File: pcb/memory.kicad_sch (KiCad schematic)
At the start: 3 parts, among them U10 MT41K256M16TW-107:P TR, U9 MX25L12835F

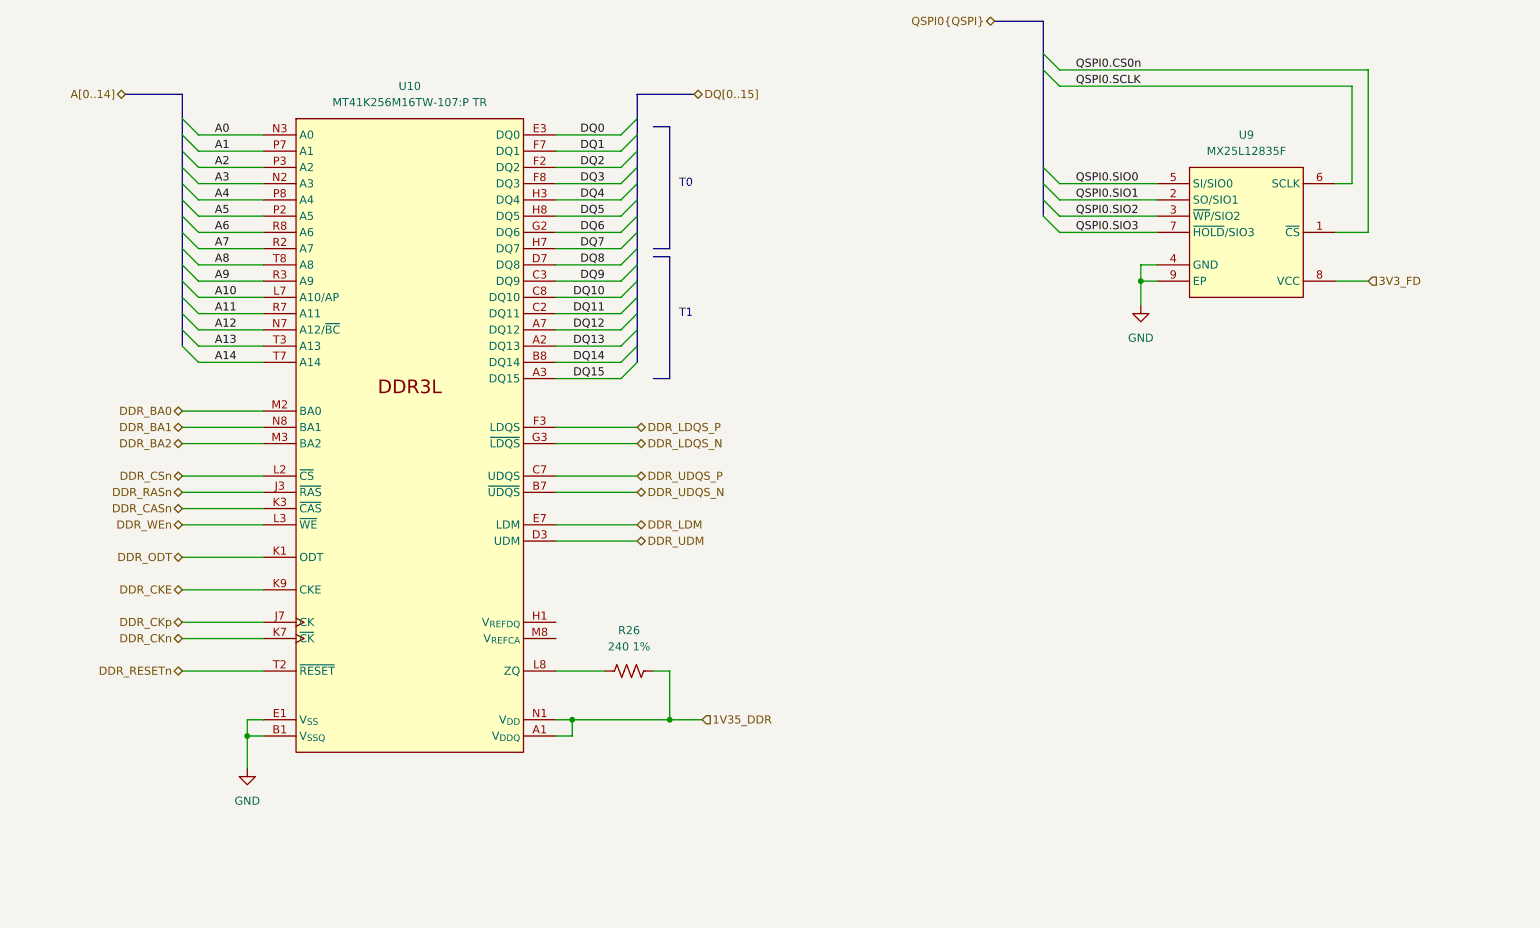
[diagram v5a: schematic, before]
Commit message: real ddr pinout done
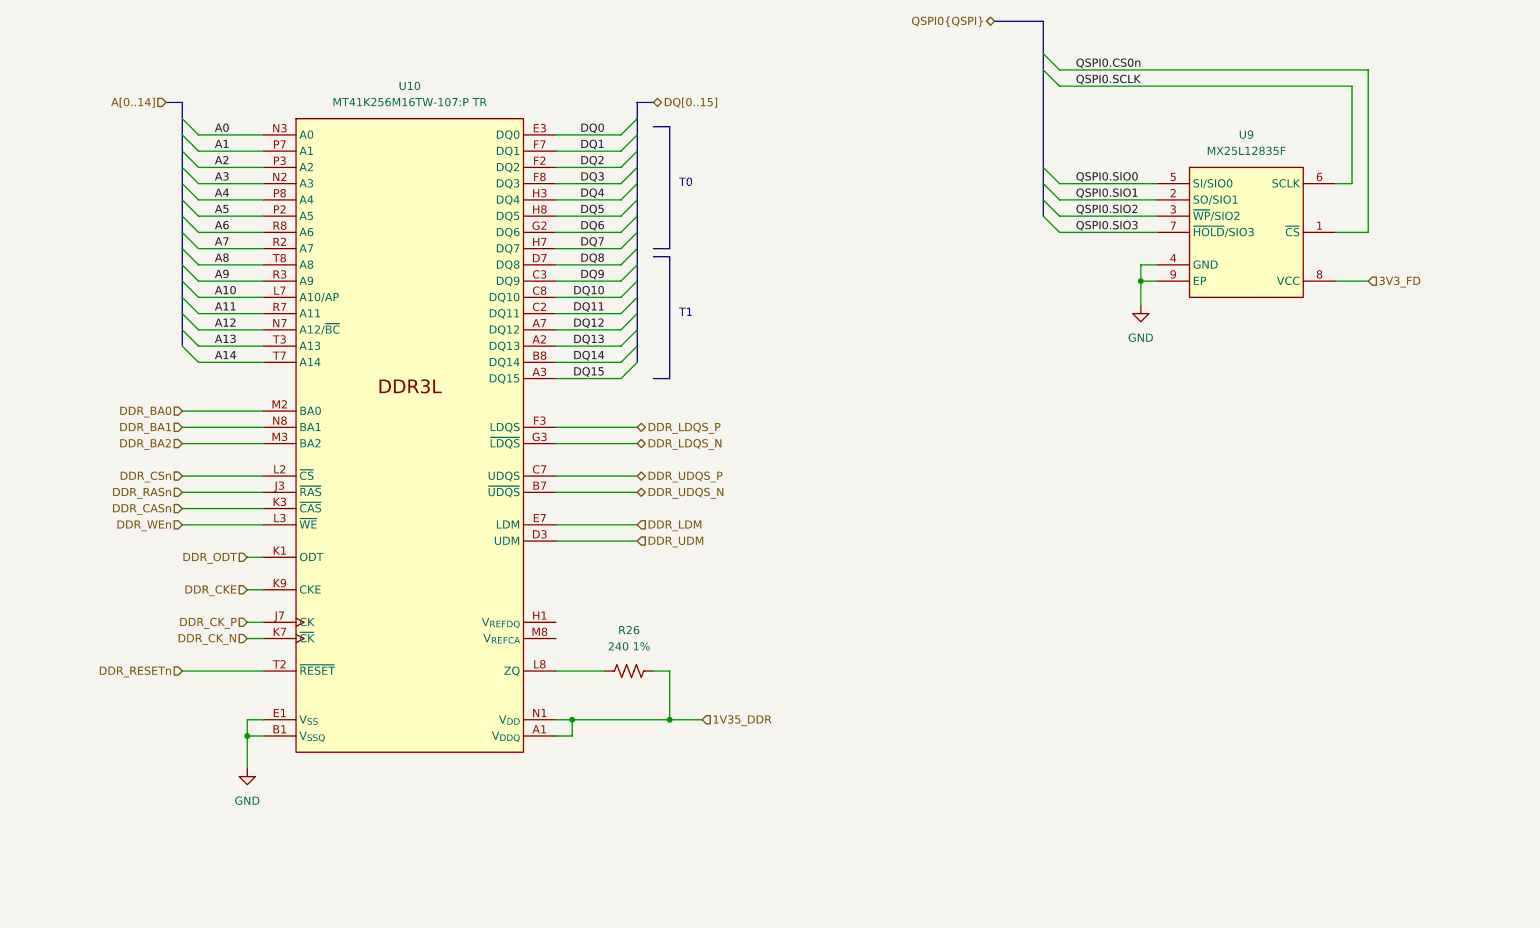
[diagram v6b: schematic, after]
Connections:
- net DDR_CKn renamed DDR_CK_N
- net DDR_CKp renamed DDR_CK_P
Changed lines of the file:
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@@
 	(wire
 		(pts
-			(xy 71.12 114.3) (xy 83.82 114.3)
+			(xy 81.28 114.3) (xy 83.82 114.3)
 		)
 		(stroke
@@
 		)
 	)
-	(bus
+	(wire
 		(pts
-			(xy 71.12 36.83) (xy 62.23 36.83)
+			(xy 73.66 76.2) (xy 83.82 76.2)
 		)
 		(stroke
@@
 		)
 	)
-	(wire
+	(bus
 		(pts
-			(xy 73.66 76.2) (xy 83.82 76.2)
+			(xy 142.24 38.1) (xy 142.24 40.64)
 		)
 		(stroke
@@
 	(wire
 		(pts
-			(xy 71.12 121.92) (xy 83.82 121.92)
+			(xy 81.28 121.92) (xy 83.82 121.92)
 		)
 		(stroke
@@
 	(wire
 		(pts
-			(xy 71.12 109.22) (xy 83.82 109.22)
+			(xy 81.28 109.22) (xy 83.82 109.22)
 		)
 		(stroke
@@
 		)
 	)
-	(bus
-		(pts
-			(xy 142.24 40.64) (xy 142.24 36.83)
-		)
-		(stroke
-			(width 0)
-			(type default)
-		)
-	)
 	(wire
 		(pts
@@
 	(bus
 		(pts
-			(xy 142.24 36.83) (xy 151.13 36.83)
-		)
-		(stroke
-			(width 0)
-			(type default)
-		)
-	)
-	(bus
-		(pts
 			(xy 142.24 63.5) (xy 142.24 60.96)
 		)
@@
 	(bus
 		(pts
-			(xy 71.12 40.64) (xy 71.12 36.83)
+			(xy 71.12 40.64) (xy 71.12 38.1)
 		)
 		(stroke
@@
 	(bus
 		(pts
+			(xy 68.58 38.1) (xy 71.12 38.1)
+		)
+		(stroke
+			(width 0)
+			(type default)
+		)
+	)
+	(bus
+		(pts
 			(xy 71.12 48.26) (xy 71.12 45.72)
 		)
@@
 		)
 	)
+	(bus
+		(pts
+			(xy 142.24 38.1) (xy 144.78 38.1)
+		)
+		(stroke
+			(width 0)
+			(type default)
+		)
+	)
 	(wire
 		(pts
@@
 	(wire
 		(pts
-			(xy 71.12 119.38) (xy 83.82 119.38)
+			(xy 81.28 119.38) (xy 83.82 119.38)
 		)
 		(stroke
@@
 		)
 	)
-	(hierarchical_label "DDR_UDM"
-		(shape bidirectional)
-		(at 142.24 106.68 0)
+	(hierarchical_label "DDR_BA0"
+		(shape input)
+		(at 71.12 86.36 180)
 		(effects
 			(font
 				(size 1.27 1.27)
 			)
-			(justify left)
+			(justify right)
 		)
 	)
-	(hierarchical_label "DDR_BA2"
+	(hierarchical_label "DQ[0..15]"
 		(shape bidirectional)
-		(at 71.12 91.44 180)
+		(at 144.78 38.1 0)
 		(effects
 			(font
 				(size 1.27 1.27)
+				(thickness 0.1588)
 			)
-			(justify right)
+			(justify left)
 		)
 	)
-	(hierarchical_label "A[0..14]"
-		(shape bidirectional)
-		(at 62.23 36.83 180)
+	(hierarchical_label "DDR_LDM"
+		(shape input)
+		(at 142.24 104.14 0)
 		(effects
 			(font
 				(size 1.27 1.27)
-				(thickness 0.1588)
 			)
-			(justify right)
+			(justify left)
 		)
 	)
-	(hierarchical_label "DDR_LDQS_P"
+	(hierarchical_label "DDR_UDQS_N"
 		(shape bidirectional)
-		(at 142.24 88.9 0)
+		(at 142.24 99.06 0)
 		(effects
 			(font
@@
 		)
 	)
-	(hierarchical_label "DDR_BA0"
-		(shape bidirectional)
-		(at 71.12 86.36 180)
+	(hierarchical_label "DDR_WEn"
+		(shape input)
+		(at 71.12 104.14 180)
 		(effects
 			(font
@@
 		)
 	)
-	(hierarchical_label "DDR_ODT"
-		(shape bidirectional)
-		(at 71.12 109.22 180)
+	(hierarchical_label "DDR_CSn"
+		(shape input)
+		(at 71.12 96.52 180)
 		(effects
 			(font
@@
 		)
 	)
-	(hierarchical_label "DDR_BA1"
-		(shape bidirectional)
-		(at 71.12 88.9 180)
+	(hierarchical_label "DDR_CK_N"
+		(shape input)
+		(at 81.28 121.92 180)
 		(effects
 			(font
@@
 		)
 	)
-	(hierarchical_label "DDR_RASn"
-		(shape bidirectional)
-		(at 71.12 99.06 180)
+	(hierarchical_label "A[0..14]"
+		(shape input)
+		(at 68.58 38.1 180)
 		(effects
 			(font
 				(size 1.27 1.27)
+				(thickness 0.1588)
 			)
 			(justify right)
 		)
 	)
-	(hierarchical_label "DDR_CKp"
-		(shape bidirectional)
-		(at 71.12 119.38 180)
+	(hierarchical_label "DDR_BA2"
+		(shape input)
+		(at 71.12 91.44 180)
 		(effects
 			(font
@@
 		)
 	)
-	(hierarchical_label "DQ[0..15]"
-		(shape bidirectional)
-		(at 151.13 36.83 0)
+	(hierarchical_label "1V35_DDR"
+		(shape input)
+		(at 152.4 134.62 0)
 		(effects
 			(font
 				(size 1.27 1.27)
-				(thickness 0.1588)
 			)
 			(justify left)
 		)
 	)
-	(hierarchical_label "DDR_WEn"
-		(shape bidirectional)
-		(at 71.12 104.14 180)
+	(hierarchical_label "DDR_BA1"
+		(shape input)
+		(at 71.12 88.9 180)
 		(effects
 			(font
@@
 		)
 	)
-	(hierarchical_label "DDR_LDQS_N"
-		(shape bidirectional)
-		(at 142.24 91.44 0)
-		(effects
-			(font
-				(size 1.27 1.27)
-			)
-			(justify left)
-		)
-	)
-	(hierarchical_label "DDR_UDQS_P"
-		(shape bidirectional)
-		(at 142.24 96.52 0)
+	(hierarchical_label "DDR_RESETn"
+		(shape input)
+		(at 71.12 127 180)
 		(effects
 			(font
 				(size 1.27 1.27)
 			)
-			(justify left)
+			(justify right)
 		)
 	)
-	(hierarchical_label "1V35_DDR"
+	(hierarchical_label "DDR_ODT"
 		(shape input)
-		(at 152.4 134.62 0)
+		(at 81.28 109.22 180)
 		(effects
 			(font
 				(size 1.27 1.27)
 			)
-			(justify left)
+			(justify right)
 		)
 	)
-	(hierarchical_label "DDR_UDQS_N"
+	(hierarchical_label "DDR_LDQS_P"
 		(shape bidirectional)
-		(at 142.24 99.06 0)
+		(at 142.24 88.9 0)
 		(effects
 			(font
@@
 		)
 	)
-	(hierarchical_label "DDR_LDM"
-		(shape bidirectional)
-		(at 142.24 104.14 0)
+	(hierarchical_label "DDR_CASn"
+		(shape input)
+		(at 71.12 101.6 180)
 		(effects
 			(font
 				(size 1.27 1.27)
 			)
-			(justify left)
+			(justify right)
 		)
 	)
-	(hierarchical_label "DDR_CSn"
-		(shape bidirectional)
-		(at 71.12 96.52 180)
+	(hierarchical_label "DDR_RASn"
+		(shape input)
+		(at 71.12 99.06 180)
 		(effects
 			(font
@@
 		)
 	)
-	(hierarchical_label "DDR_CKE"
+	(hierarchical_label "DDR_UDQS_P"
 		(shape bidirectional)
-		(at 71.12 114.3 180)
+		(at 142.24 96.52 0)
 		(effects
 			(font
 				(size 1.27 1.27)
 			)
-			(justify right)
+			(justify left)
 		)
 	)
-	(hierarchical_label "DDR_CASn"
+	(hierarchical_label "DDR_LDQS_N"
 		(shape bidirectional)
-		(at 71.12 101.6 180)
+		(at 142.24 91.44 0)
 		(effects
 			(font
 				(size 1.27 1.27)
 			)
-			(justify right)
+			(justify left)
 		)
 	)
@@
 		)
 	)
-	(hierarchical_label "DDR_RESETn"
-		(shape bidirectional)
-		(at 71.12 127 180)
+	(hierarchical_label "DDR_CKE"
+		(shape input)
+		(at 81.28 114.3 180)
 		(effects
 			(font
@@
 		)
 	)
-	(hierarchical_label "DDR_CKn"
-		(shape bidirectional)
-		(at 71.12 121.92 180)
+	(hierarchical_label "DDR_UDM"
+		(shape input)
+		(at 142.24 106.68 0)
+		(effects
+			(font
+				(size 1.27 1.27)
+			)
+			(justify left)
+		)
+	)
+	(hierarchical_label "DDR_CK_P"
+		(shape input)
+		(at 81.28 119.38 180)
 		(effects
 			(font

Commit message: restructured power, power plane layout
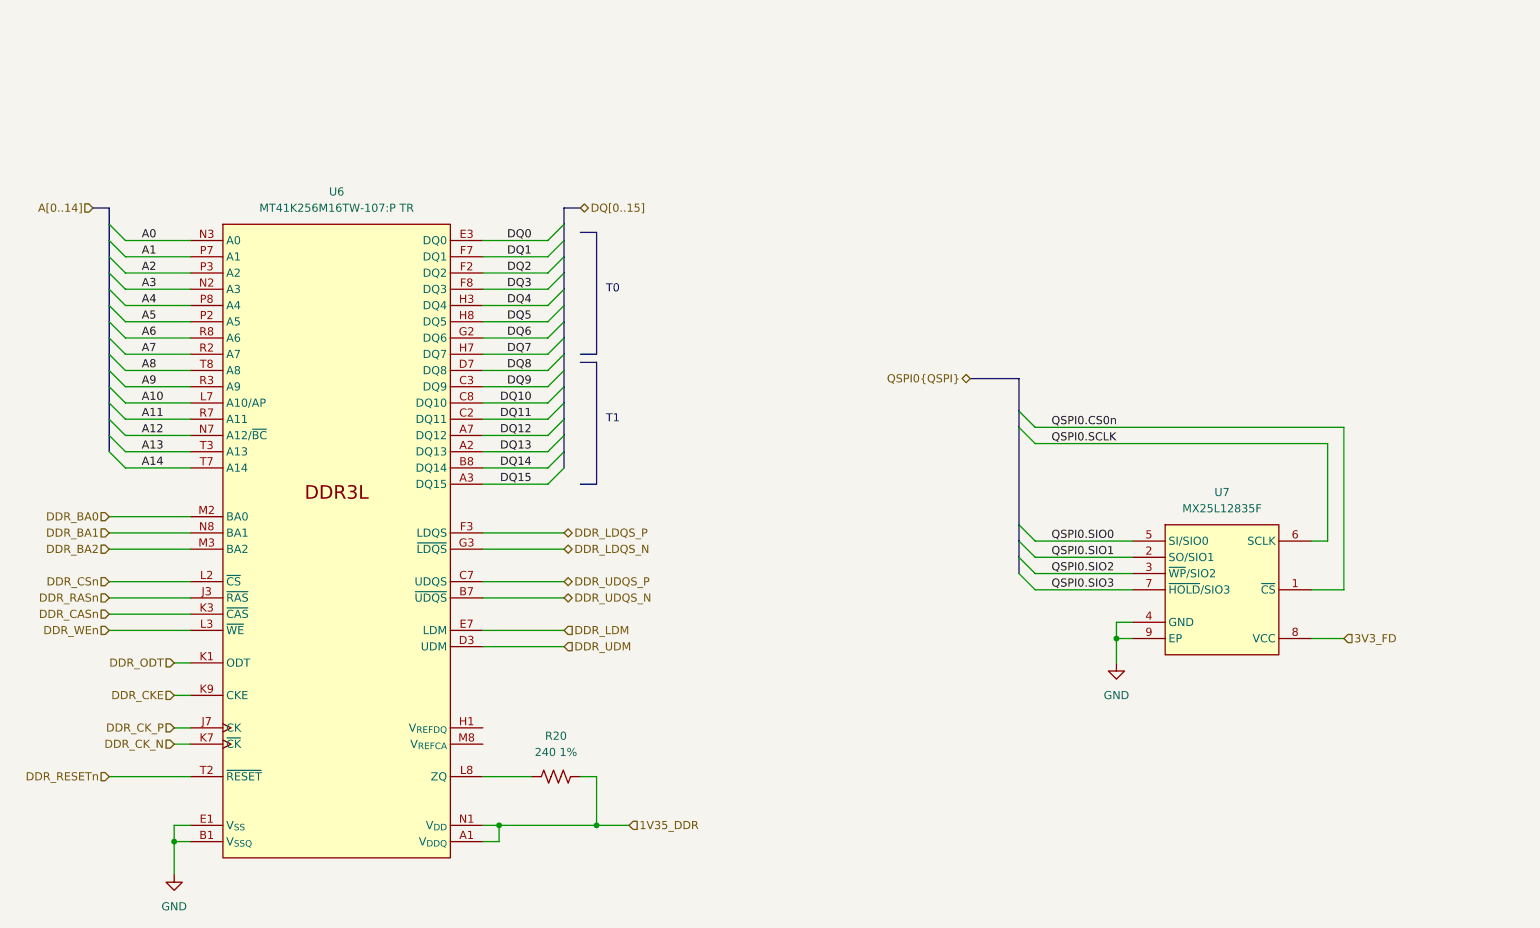
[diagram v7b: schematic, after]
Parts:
- renumbered R26 to R20, U10 to U6, U9 to U7
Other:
- moved on the sheet: R20, U6, U7

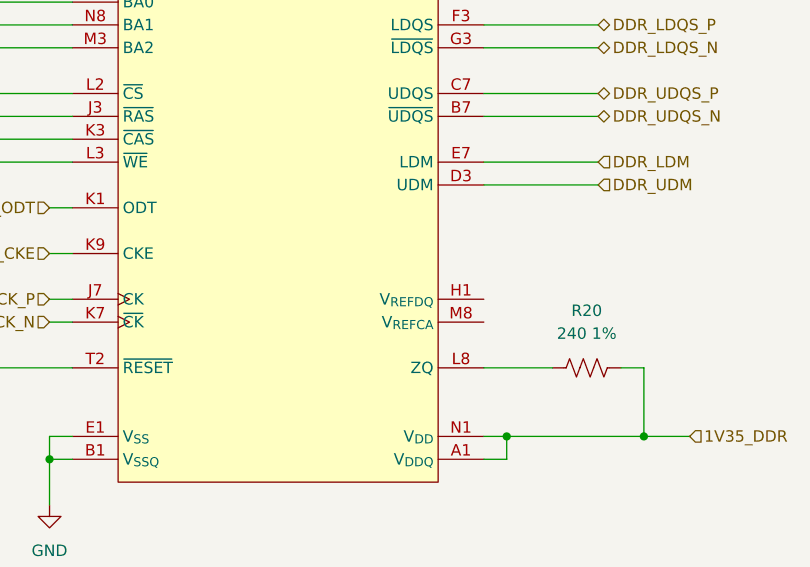
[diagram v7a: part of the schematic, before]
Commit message: dogbone for ddr
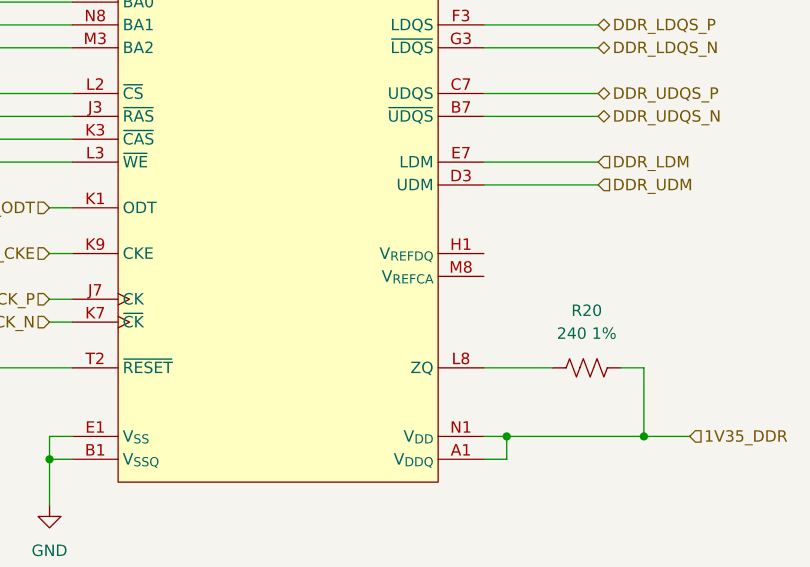
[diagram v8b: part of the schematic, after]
